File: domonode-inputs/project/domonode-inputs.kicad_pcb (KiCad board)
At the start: 2 copper layers, 95 x 80 mm, 66 parts, among them P1 CONN_01X02, P10 CONN_01X02, P11 CONN_01X02, P12 CONN_02X03, P13 CONN_02X05, P14 CONN_01X06, P2 CONN_01X02, P3 CONN_01X02, P4 CONN_01X02, P5 CONN_01X02, P6 CONN_01X02, P7 CONN_01X02, P8 CONN_01X02, P9 CONN_01X02, U1 TLP620, U10 TLP620, U11 PCA9555, U12 24LC02, U13 TLP620, U2 TLP620, U3 TLP620, U4 TLP620, U5 TLP620, U6 TLP620, U7 TLP620, U8 TLP620, U9 TLP620

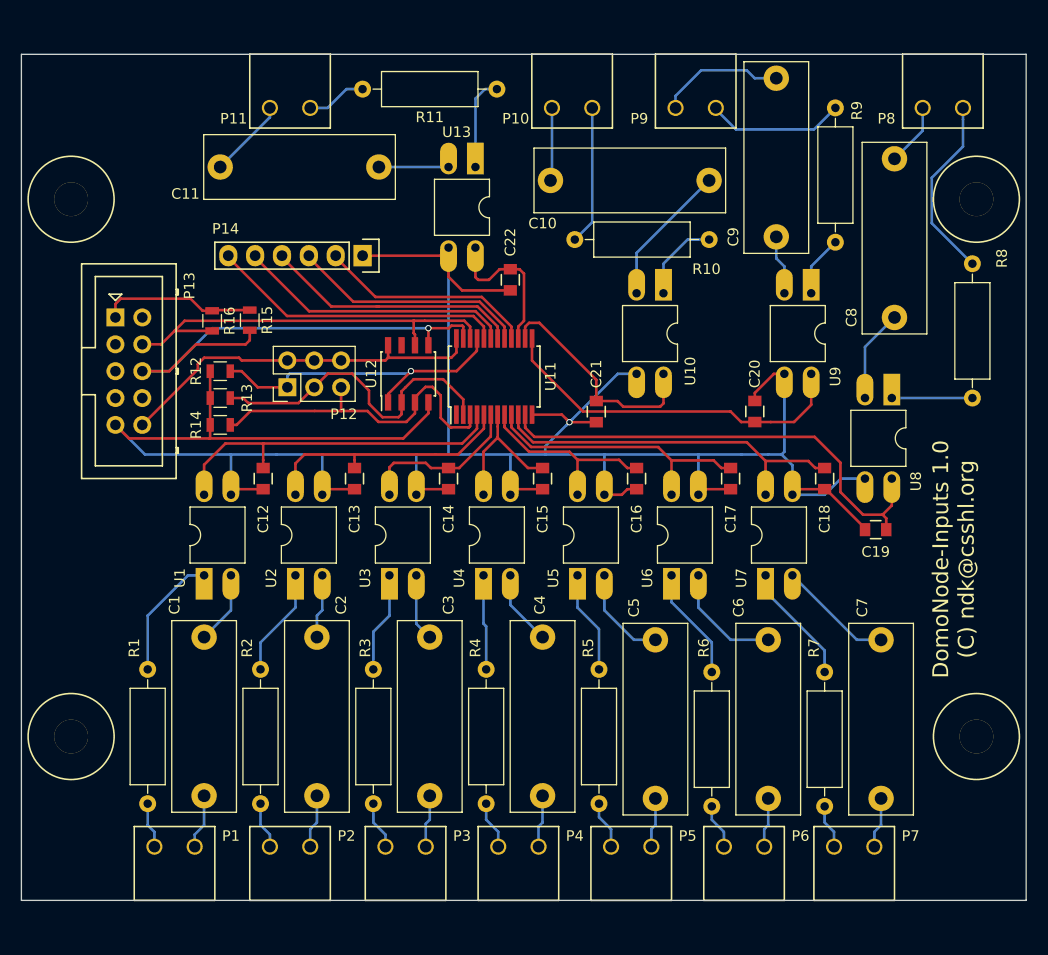
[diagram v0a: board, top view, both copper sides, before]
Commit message: Renamed domonode-inputs project files, replaced connectors, reduced isolation for 230V to 1.5mm (requires a PCB with solder mask)
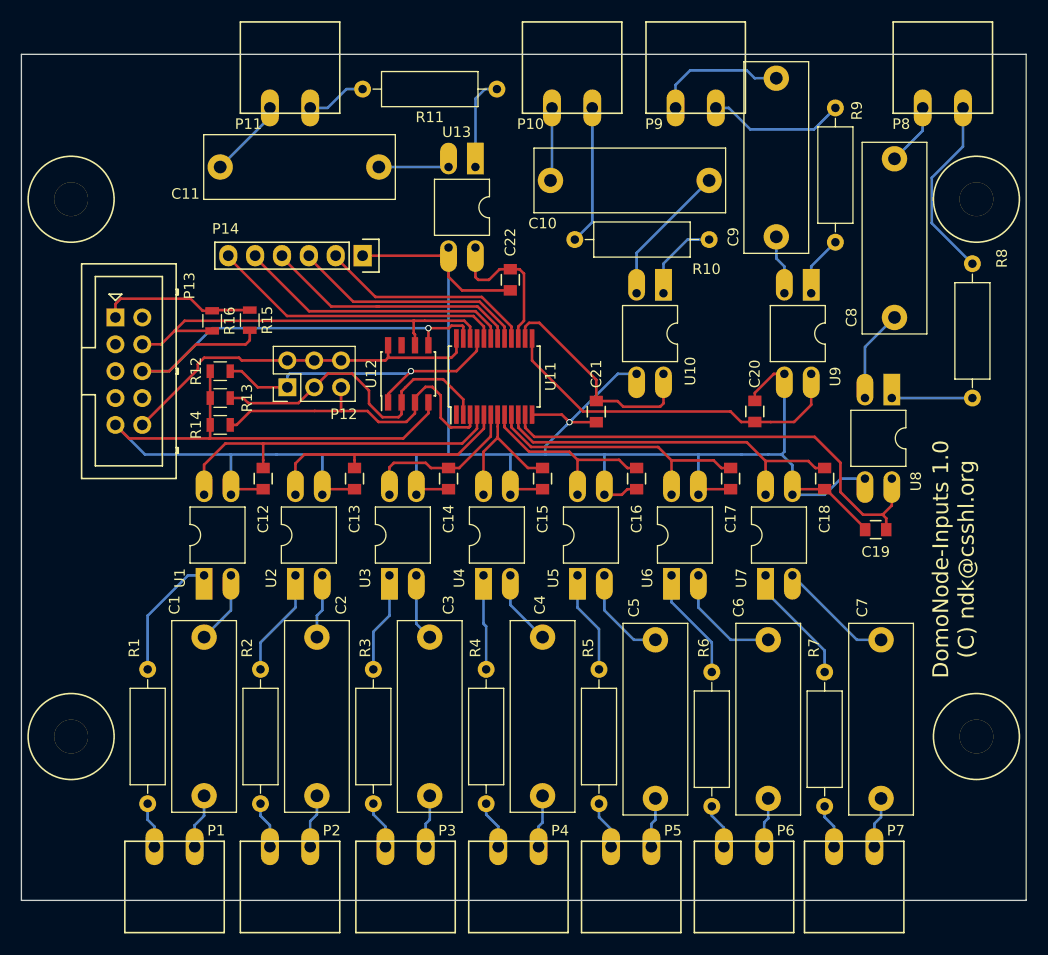
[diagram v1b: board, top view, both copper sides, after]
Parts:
- P1, P10, P11, P2, P3, P4, P5, P6, P7, P8, P9: footprint AAA mie lib verificate:ScrewTerm_2x3.81_big_holes -> AAA mie lib verificate:KF2EDGK-3.81-2
- moved P1 1.91 mm to (156.6, 101.3)
- moved P10 1.91 mm to (190.4, 31.5)
- moved P11 1.91 mm to (163.7, 31.5)
- moved P2 1.91 mm to (167.5, 101.3)
- moved P3 1.91 mm to (178.4, 101.3)
- moved P4 1.91 mm to (189.1, 101.3)
- moved P6 1.91 mm to (210.4, 101.3)
- moved P7 1.91 mm to (220.9, 101.3)
- moved P8 1.91 mm to (225.4, 31.5)
- moved P9 1.91 mm to (202.1, 31.5)
- moved P5 1.90 mm to (199.8, 101.3)
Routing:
- net Net-(C9-Pad2): track 12.0 -> 12.6 mm
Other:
- net class 220V: clearance 2.5 -> 1.5
